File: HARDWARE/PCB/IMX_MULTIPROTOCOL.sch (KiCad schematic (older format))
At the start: 16 parts, among them J17 Conn_01x08, J18 Conn_01x06, J19 Conn_01x10, J20 Conn_01x08

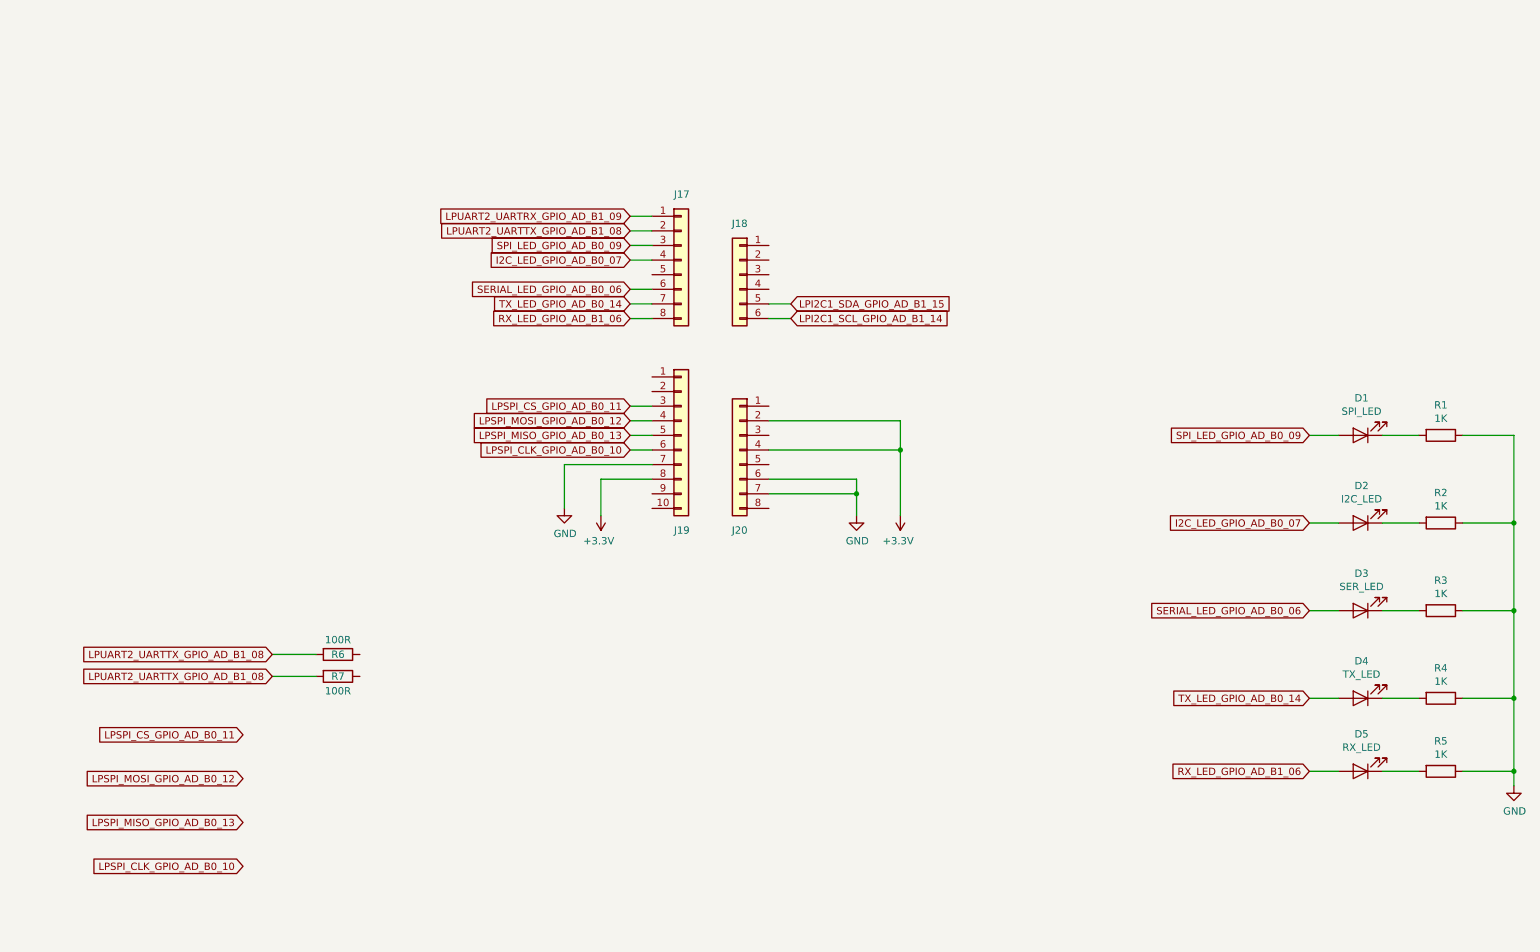
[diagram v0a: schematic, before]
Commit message: FIRMWARE: USB fix, Led rework,
HARDWARE: Led rework
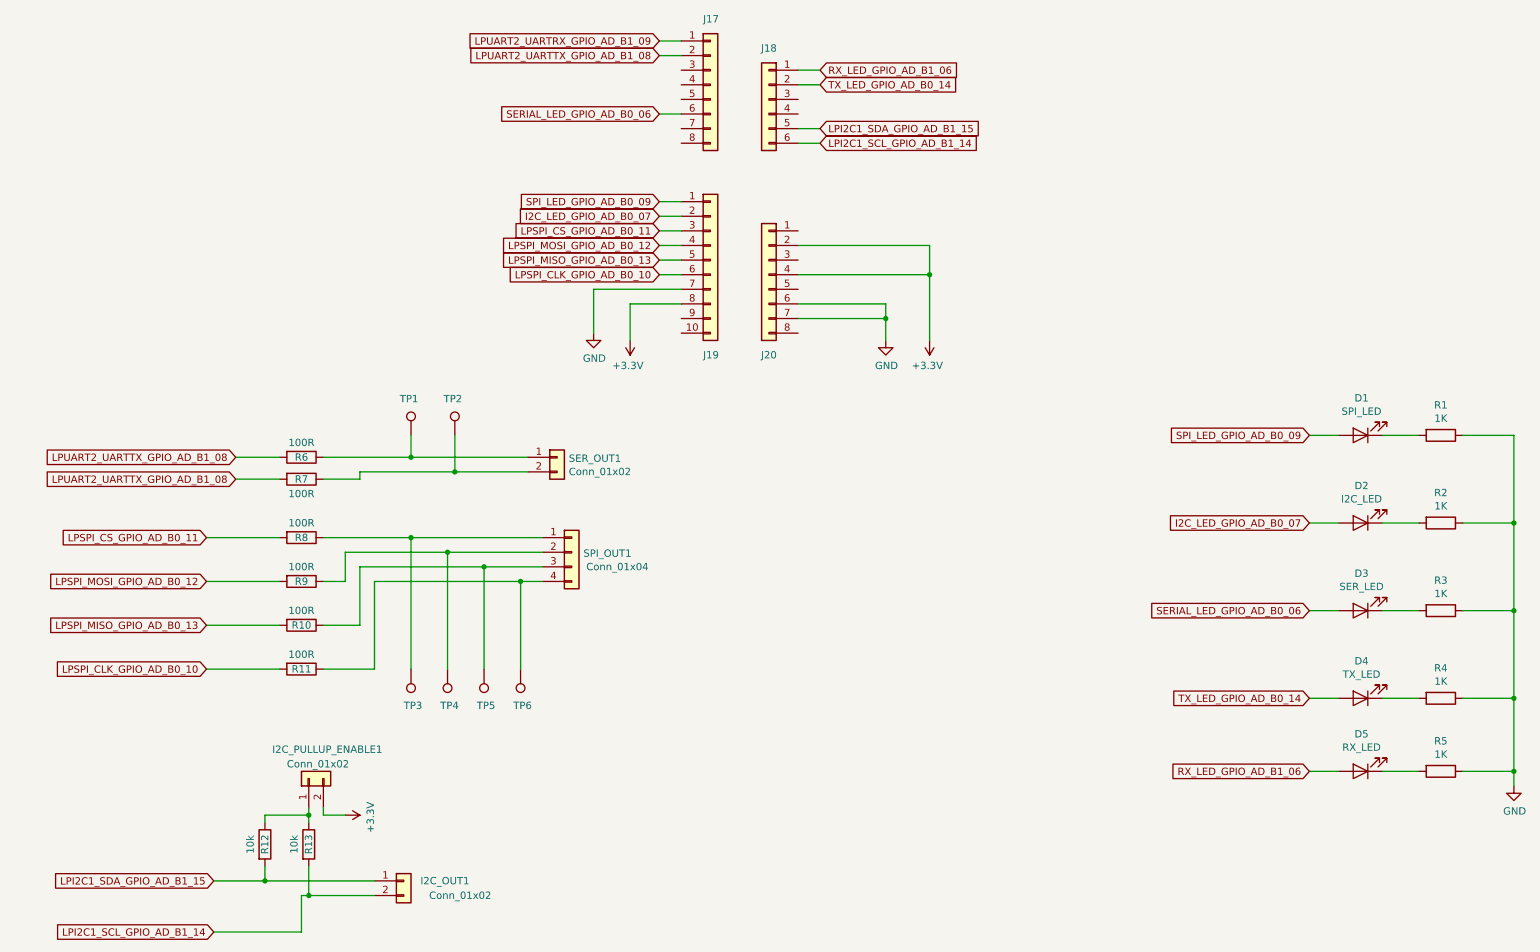
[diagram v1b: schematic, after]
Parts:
- added I2C_OUT1, I2C_PULLUP_ENABLE1, SER_OUT1: Conn_01x02, Connector_PinHeader_2.54mm:PinHeader_1x02_P2.54mm_Vertical, symbol Connector_Generic:Conn_01x02
- added R10, R11, R8, R9: 100R, Resistor_SMD:R_0805_2012Metric_Pad1.15x1.40mm_HandSolder, symbol Device:R
- added R12, R13: 10k, Resistor_SMD:R_0805_2012Metric_Pad1.15x1.40mm_HandSolder, symbol Device:R
- added SPI_OUT1: Conn_01x04, Connector_PinHeader_2.54mm:PinHeader_1x04_P2.54mm_Vertical, symbol Connector_Generic:Conn_01x04
- added TP1, TP2, TP3, TP4, TP5, TP6: TestPoint, TestPoint:TestPoint_Pad_D1.5mm, symbol Connector:TestPoint
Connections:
- net +3V3: now also I2C_PULLUP_ENABLE1.2 (Pin_2)
- net I2C_LED_GPIO_AD_B0_07: now also J19.2 (Pin_2); no longer J17.4 (Pin_4)
- net LPI2C1_SCL_GPIO_AD_B1_14: now also I2C_OUT1.2 (Pin_2), R13.2
- net LPI2C1_SDA_GPIO_AD_B1_15: now also I2C_OUT1.1 (Pin_1), R12.2
- net LPSPI_CLK_GPIO_AD_B0_10: now also R11.2
- net LPSPI_CS_GPIO_AD_B0_11: now also R8.2
- net LPSPI_MISO_GPIO_AD_B0_13: now also R10.2
- net LPSPI_MOSI_GPIO_AD_B0_12: now also R9.2
- net RX_LED_GPIO_AD_B1_06: now also J18.1 (Pin_1); no longer J17.8 (Pin_8)
- net SPI_LED_GPIO_AD_B0_09: now also J19.1 (Pin_1); no longer J17.3 (Pin_3)
- net TX_LED_GPIO_AD_B0_14: now also J18.2 (Pin_2); no longer J17.7 (Pin_7)
- net at R6.1: now also SER_OUT1.1 (Pin_1), TP1.1
- net at R7.1: now also SER_OUT1.2 (Pin_2), TP2.1
- new net: R8.1, SPI_OUT1.1 (Pin_1), TP3.1
- new net: R9.1, SPI_OUT1.2 (Pin_2), TP4.1
- new net: R10.1, SPI_OUT1.3 (Pin_3), TP5.1
- new net: R11.1, SPI_OUT1.4 (Pin_4), TP6.1
- new net: I2C_PULLUP_ENABLE1.1 (Pin_1), R12.1, R13.1
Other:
- moved on the sheet: J17, J18, J19, J20, R6, R7
